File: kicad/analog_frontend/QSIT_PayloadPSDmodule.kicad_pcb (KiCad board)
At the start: 4 copper layers, 36 x 36 mm, 60 parts, among them J1 Conn_02x05_Odd_Even, J2 Conn_02x05_Odd_Even, J3 Conn_02x05_Odd_Even, U1 PSDS5990-01, U2 OPA4990IRTER, U3 OPA4990IRTER, U4 OPA4990IRTER, U5 OPA4990IRTER

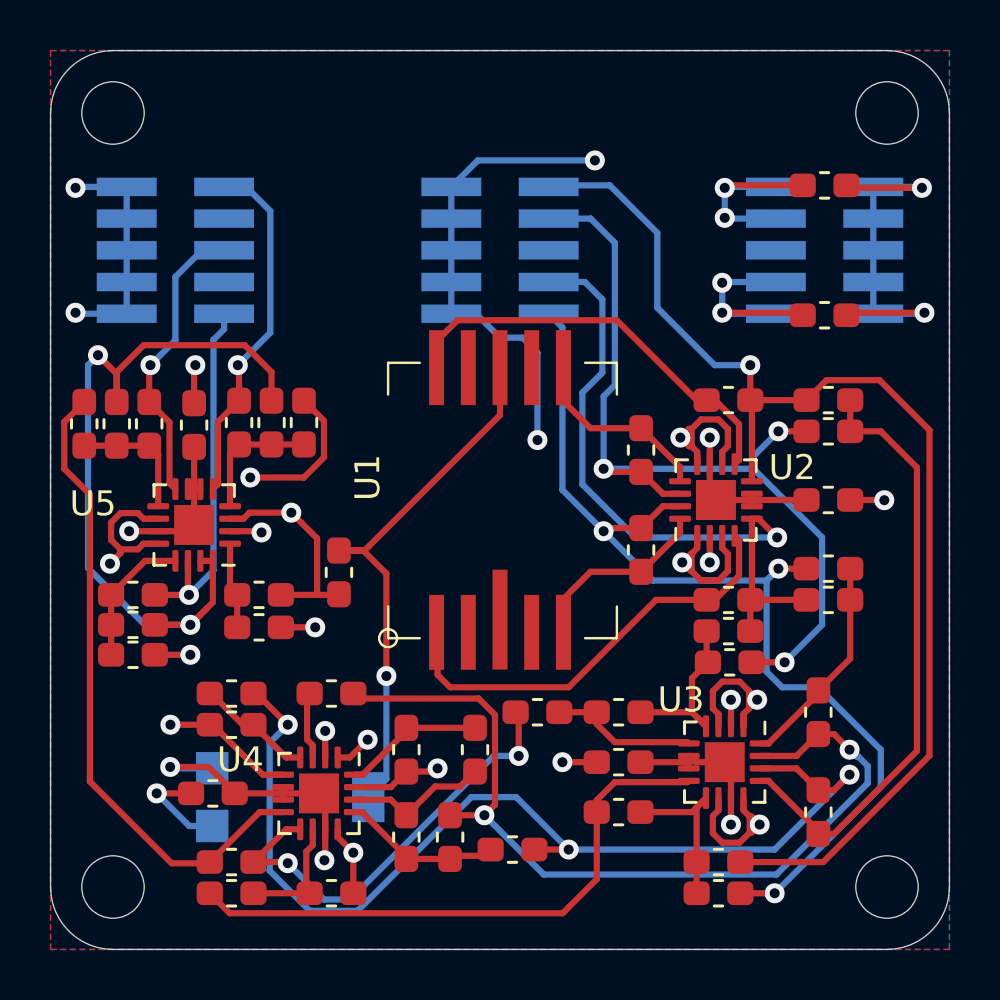
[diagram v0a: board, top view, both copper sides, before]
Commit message: added stm32f373cct6
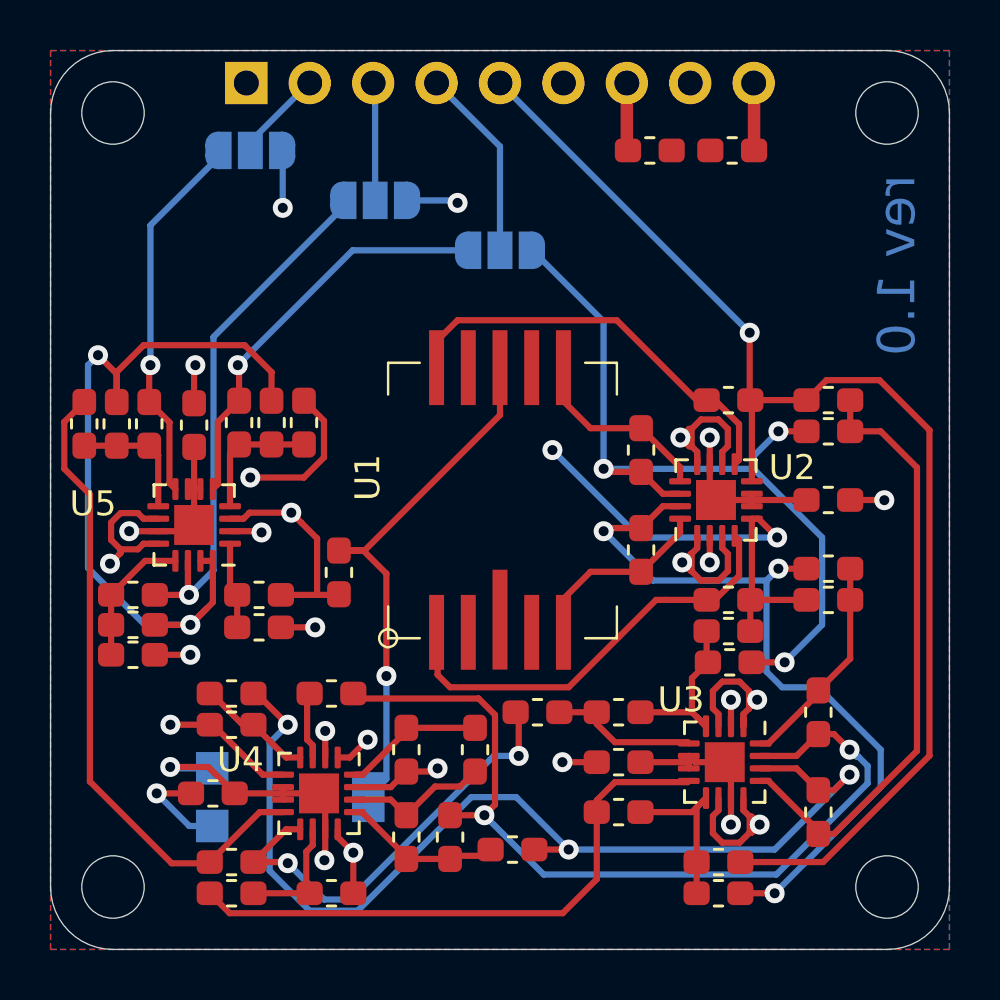
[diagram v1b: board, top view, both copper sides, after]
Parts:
- removed J2, J3: Conn_02x05_Odd_Even, Connector_PinHeader_1.27mm:PinHeader_2x05_P1.27mm_Vertical_SMD
- added JP1: bridge, Jumper:SolderJumper-3_P1.3mm_Open_RoundedPad1.0x1.5mm, B.Cu at (130.0, 103.0)
- added JP2: bridge, Jumper:SolderJumper-3_P1.3mm_Open_RoundedPad1.0x1.5mm, B.Cu at (120.0, 99.0)
- added JP3: bridge, Jumper:SolderJumper-3_P1.3mm_Open_RoundedPad1.0x1.5mm, B.Cu at (125.0, 101.0)
- J1: value Conn_02x05_Odd_Even -> Conn_01x09; footprint Connector_PinHeader_1.27mm:PinHeader_2x05_P1.27mm_Vertical_SMD -> Connector_PinHeader_2.54mm:PinHeader_1x09_P2.54mm_Vertical
- moved J1 24.1 mm to (119.8, 96.3), turned to 270 degrees
- moved H5 12.1 mm to (125.1, 108.3)
- moved C7 7.57 mm to (139.3, 99.0), turned to 180 degrees
- moved C6 7.14 mm to (136.0, 99.0)
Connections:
- J1 pad 1: -5V -> GND
- J1 pad 2: GND -> ADC_CH4
- J1 pad 3: -5V -> ADC_CH3
- J1 pad 4: GND -> ADC_CH2
- J1 pad 5: Net-(J1-Pad5) -> ADC_CH1
- J1 pad 9: +5V -> -5V
- R1 pad 1: /Y2a -> ADC_CH1
- R2 pad 2: /Y2a -> ADC_CH1
- R6 pad 2: /Y2a -> ADC_CH1
- U2 pad 8: /Y2a -> ADC_CH1
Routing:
- net ADC_CH1: track 0.00 -> 50.8 mm, vias 0 -> 1
- net /Y2a: track 48.4 -> 0.00 mm, vias 1 -> 0
- net GND: track 86.2 -> 42.7 mm, vias 14 -> 8
- net /X1a: track 41.3 -> 52.3 mm, vias 3 -> 4
- net ADC_CH2: track 0.00 -> 7.75 mm
- net /U_signal: track 14.6 -> 21.1 mm
- net /Y1a: track 27.3 -> 32.4 mm, vias 1 -> 3
- net ADC_CH3: track 0.00 -> 4.73 mm
- net ADC_CH4: track 0.00 -> 3.70 mm
- net /X_signal: track 11.8 -> 15.1 mm
- net -5V: track 127.6 -> 130.0 mm, vias 8 -> 6
- net /X2a: track 35.6 -> 33.3 mm
- net /Y_signal: track 14.4 -> 16.5 mm
- net +5V: track 115.7 -> 114.5 mm, vias 10 -> 8
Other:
- board text added: "1"
- board text added: "2"
- board text added: "3"
- board text added: "4"
- board text added: "GND"
- board text added: "rev 1.0"
- board text removed: "X"
- board text removed: "X1"
- board text removed: "X2"
- board text removed: "Y"
- board text removed: "Y1"
- board text removed: "Y2"
- board text removed: "den"

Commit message: rev 1 finished - final check on PSD frontend - plotted gerbber for jlc - added simulation for PSD frontend
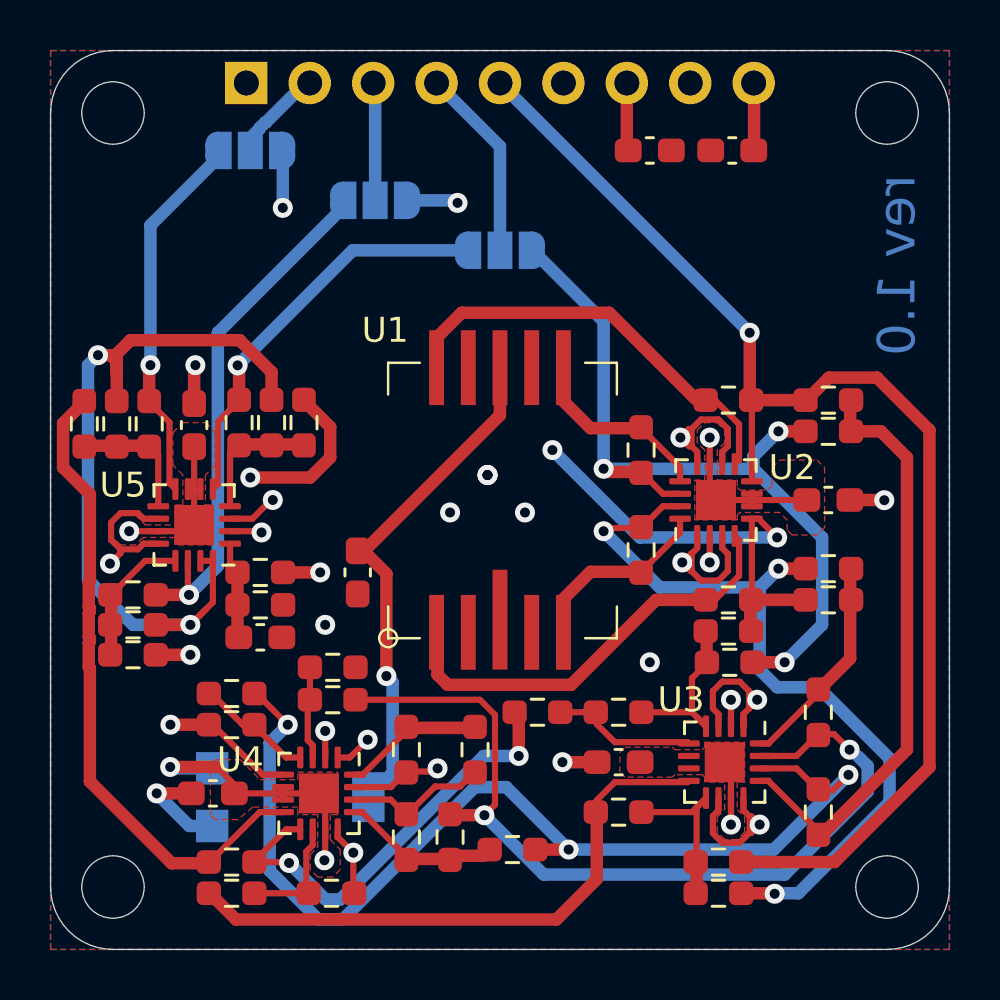
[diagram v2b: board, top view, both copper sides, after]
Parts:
- removed R33: 10k, Resistor_SMD:R_0603_1608Metric_Pad1.05x0.95mm_HandSolder
- removed R6: 4k7, Resistor_SMD:R_0603_1608Metric_Pad1.05x0.95mm_HandSolder
- added C8: 100nF, Capacitor_SMD:C_0603_1608Metric_Pad1.08x0.95mm_HandSolder, F.Cu at (120.4, 118.5)
- added R: 10k, Resistor_SMD:R_0603_1608Metric_Pad0.98x0.95mm_HandSolder, F.Cu at (115.3, 118.0)
- added R40: 4k7, Resistor_SMD:R_0603_1608Metric_Pad0.98x0.95mm_HandSolder, F.Cu at (123.3, 119.7)
- added W: 4k7, Resistor_SMD:R_0603_1608Metric_Pad0.98x0.95mm_HandSolder, F.Cu at (143.2, 109.0)
- C1, C2, C3, C4, C5, C6, C7: footprint Capacitor_SMD:C_0603_1608Metric_Pad1.05x0.95mm_HandSolder -> Capacitor_SMD:C_0603_1608Metric_Pad1.08x0.95mm_HandSolder
- R1, R10, R11, R12, R13, R14, R15, R16, R17, R18, R19, R2, R20, R21, R22, R23, R24, R25, R26, R27, R28, R29, R3, R30, R31, R32, R34, R35, R36, R37, R38, R39, R4, R5, R7, R8, R9: footprint Resistor_SMD:R_0603_1608Metric_Pad1.05x0.95mm_HandSolder -> Resistor_SMD:R_0603_1608Metric_Pad0.98x0.95mm_HandSolder
- U1: footprint A_Tale_Of_A_Library:HAMAMATSU_PSD_S599001_4mm -> simonmartin_kicad_lib:HAMAMATSU_PSD_S599001_4mm
- moved R37 2.20 mm to (120.4, 115.9)
- moved C1 0.75 mm to (124.3, 115.9)
- moved R35 0.40 mm to (120.4, 117.2)
- moved R27 0.25 mm to (123.3, 121.0)
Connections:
- net Net-(R1-Pad2) renamed /PSD_Y2
- net Net-(R10-Pad2) renamed /PSD_X1
- net Net-(R16-Pad2) renamed /PSD_Y1
- net Net-(R8-Pad2) renamed /PSD_X2
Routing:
- net GND: track 42.7 -> 36.2 mm, vias 8 -> 14
- net -5V: track 130.0 -> 124.2 mm
- net +5V: track 114.5 -> 110.6 mm
- net VAA: track 22.1 -> 20.3 mm
- net /X1a: track 52.3 -> 53.8 mm
- net /PSD_Y2: track 16.5 -> 17.9 mm
- net -2V5: track 31.1 -> 32.3 mm
- net Net-(R27-Pad1): track 2.70 -> 3.73 mm
- net /Y_n: track 23.1 -> 23.8 mm
- net Net-(R5-Pad1): track 24.5 -> 23.9 mm
- net /X2Y2: track 41.5 -> 42.0 mm
- added copper zone on F.Cu, net -5V

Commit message: fixed wrong connection to PSD X/Y axis
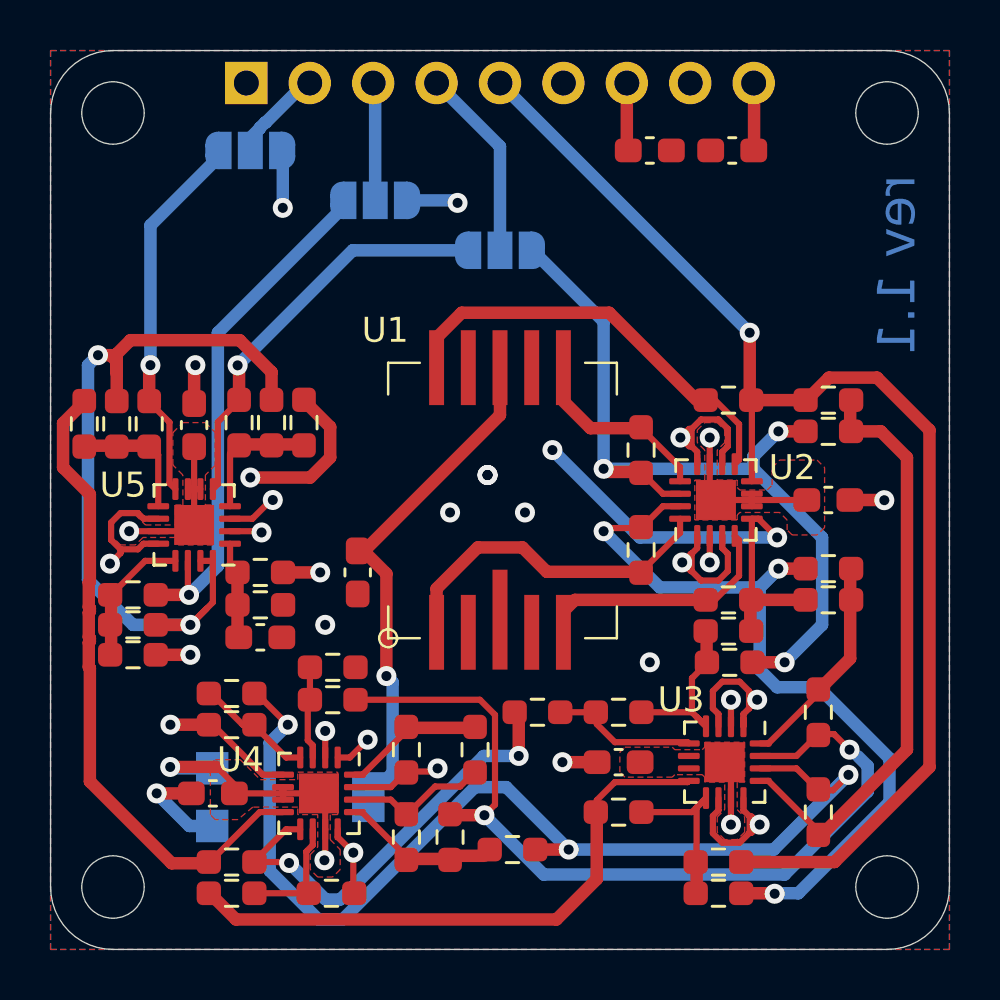
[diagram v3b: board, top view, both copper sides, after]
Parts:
- R29, R39: value 10k -> 20k
- R30, R32, R38: value 20k -> 40k
- R33: renamed from R; value 10k -> 20k
- renumbered W to R6
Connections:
- U1 pad 1: /PSD_Y1 -> /PSD_X1
- U1 pad 5: /PSD_X1 -> /PSD_Y1
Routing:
- net /PSD_Y1: track 17.4 -> 10.1 mm
- net /PSD_X1: track 7.67 -> 13.8 mm
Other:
- board text added: "rev 1.1"
- board text removed: "rev 1.0"
